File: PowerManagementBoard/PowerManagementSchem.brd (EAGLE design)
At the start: 160 x 100 mm, 100 parts, among them J1 D15S24A4GV00LF, J2 455-1750-1-ND, U1 VX7805-500, U2 PYB20-Q24-S5, U3 PYB30-Q48-S5, U4 PYB30-Q48-S12, U5 3V3REG, U6 INA4180-SPLIT, U7 INA4180-SPLIT, U8 TEENSY-4.0SILK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

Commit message: Initial board layout
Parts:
- moved U$20 793.9 mm to (161.3, 81.3), turned to 180 degrees
- moved R22 785.4 mm to (157.5, 78.7)
- moved J7 775.0 mm to (160.0, 30.5), turned to 90 degrees
- moved J6 733.6 mm to (120.7, 12.7), turned to 180 degrees
- moved J5 718.0 mm to (96.5, 12.7), turned to 180 degrees
- moved D12 712.9 mm to (128.3, 27.9), turned to 270 degrees
- moved U$23 704.2 mm to (134.6, 26.7)
- moved R21 703.1 mm to (128.3, 21.6), turned to 90 degrees
- moved D10 694.3 mm to (137.2, 41.9)
- moved J2 693.5 mm to (73.7, 12.7), turned to 180 degrees
- moved J4 692.9 mm to (53.3, 12.7), turned to 180 degrees
- moved D9 683.0 mm to (137.2, 34.3)
- moved J3 679.9 mm to (34.3, 12.7), turned to 180 degrees
- moved U9 669.6 mm to (138.4, 48.3)
- moved RN3 664.7 mm to (148.6, 27.9), turned to 180 degrees
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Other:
- board size 160 x 100 mm -> 165.1 x 106.3 mm

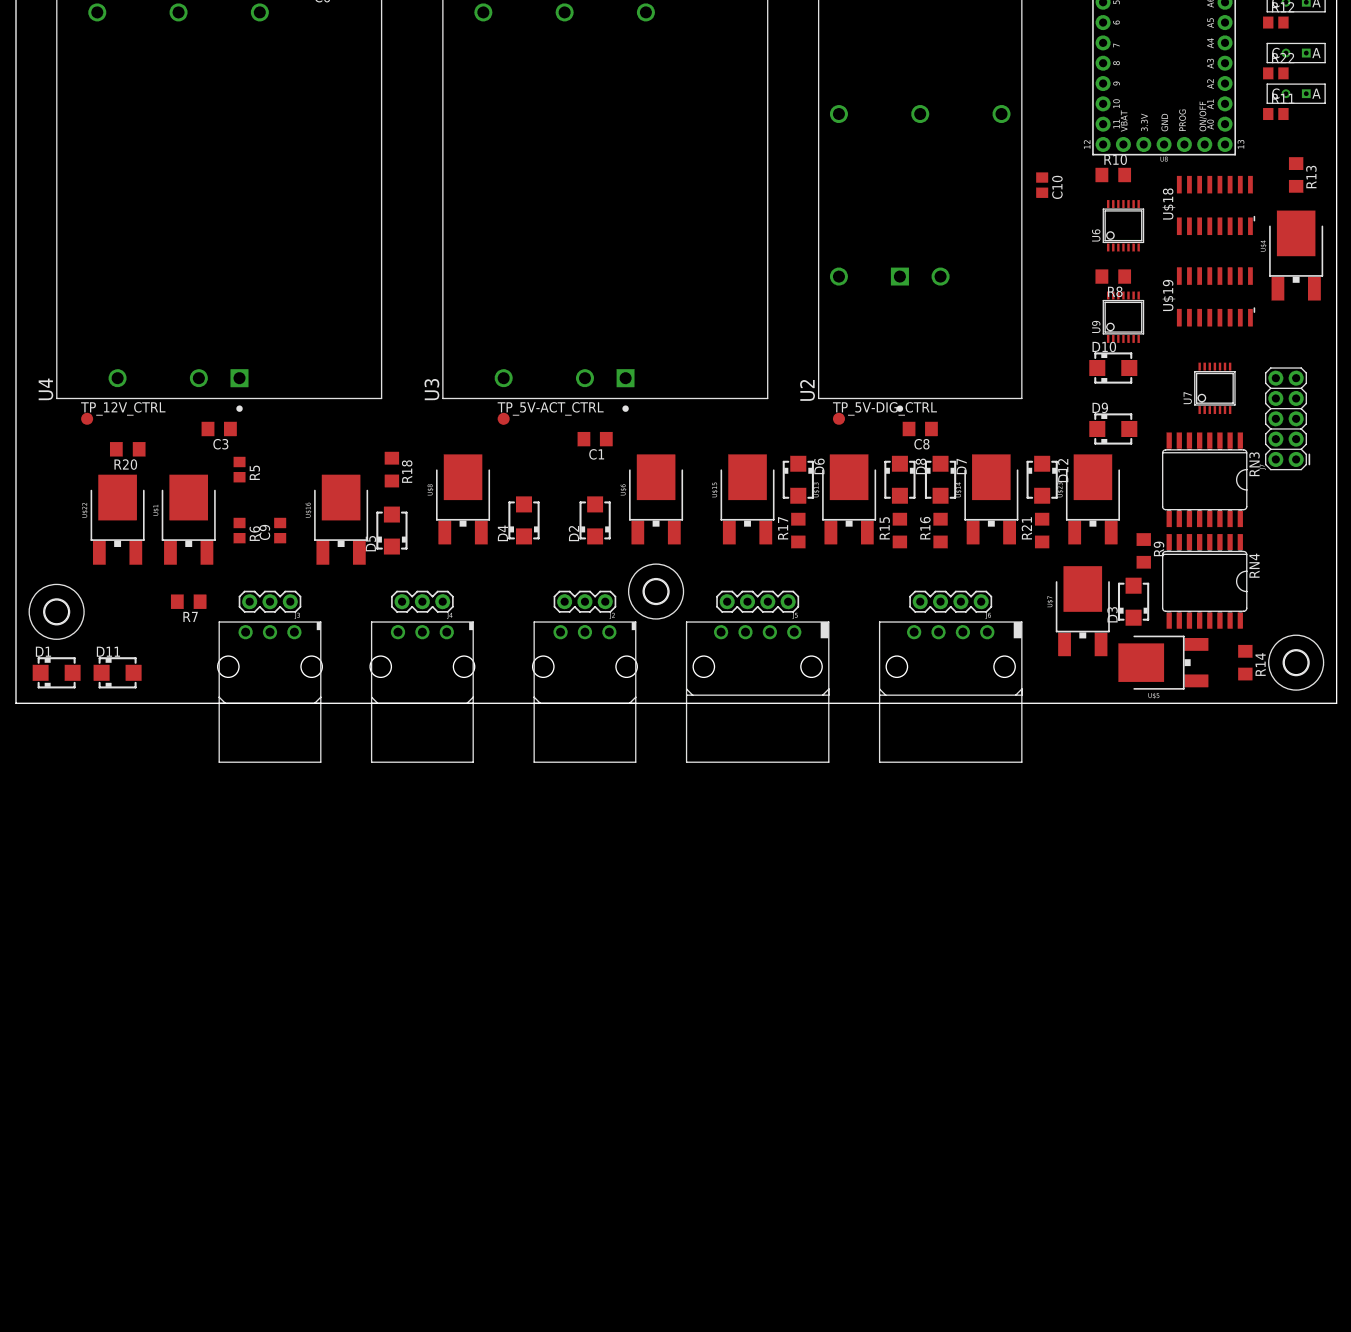
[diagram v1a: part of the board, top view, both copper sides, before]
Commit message: added db 37 and db25
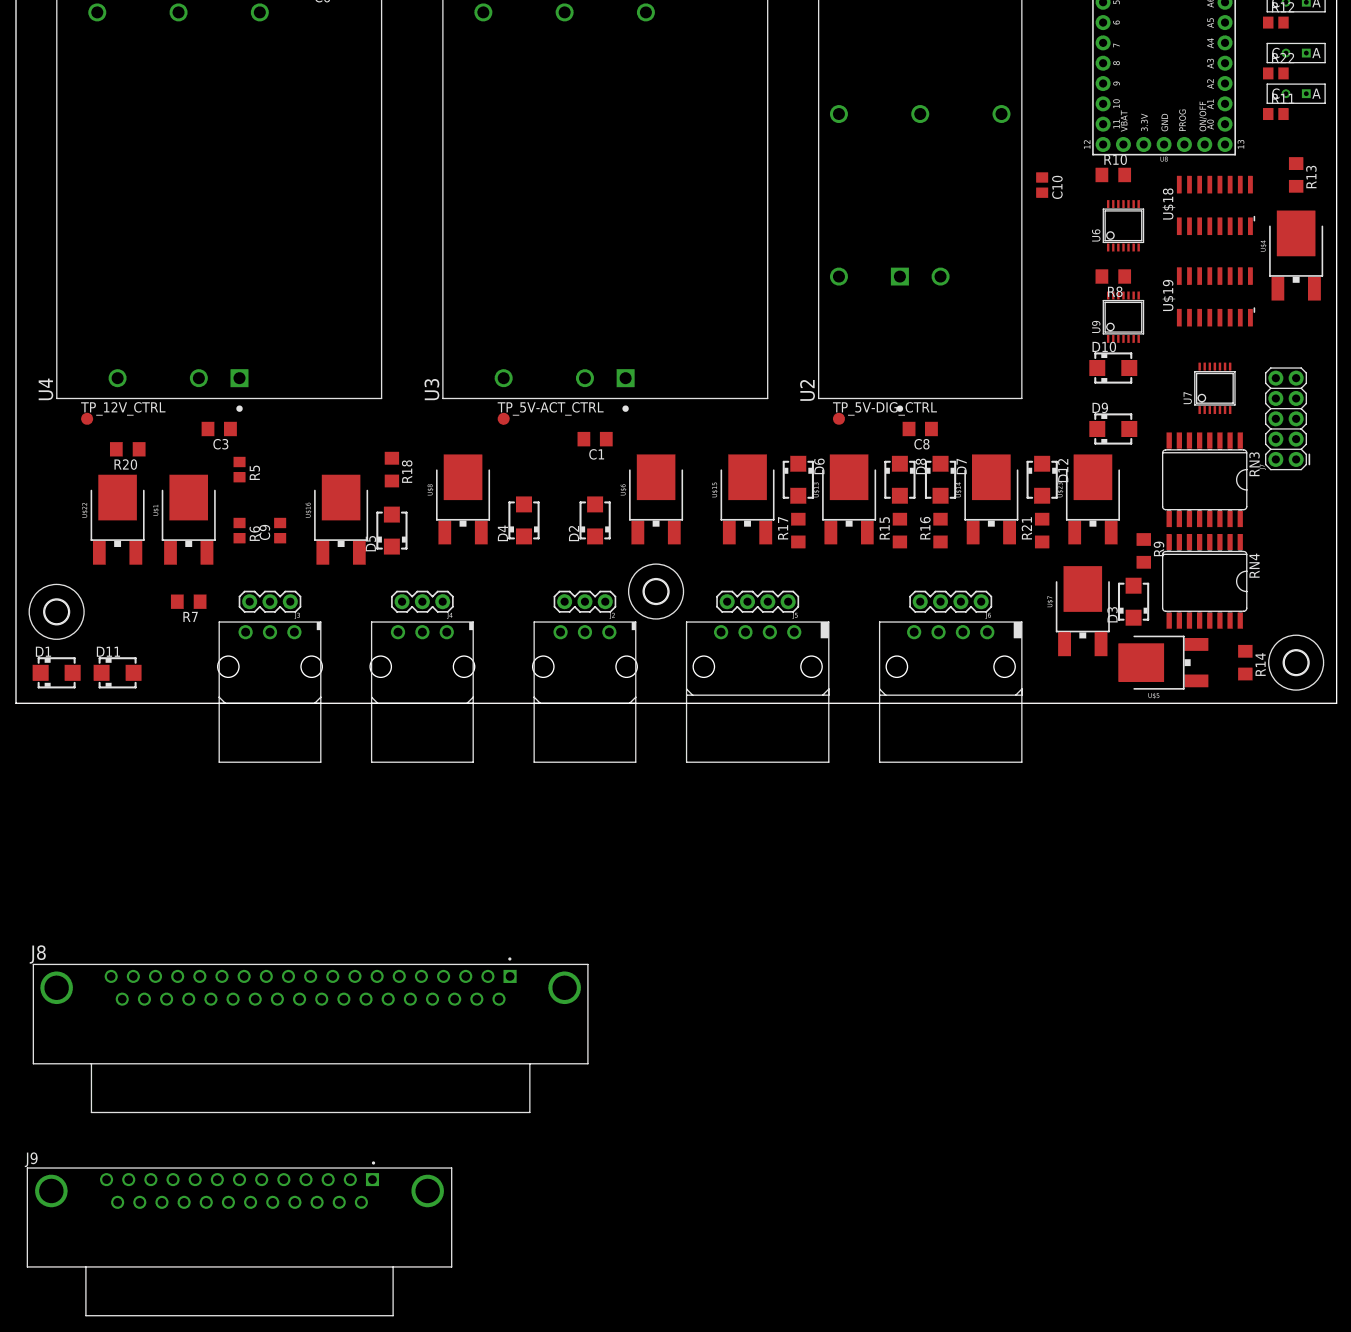
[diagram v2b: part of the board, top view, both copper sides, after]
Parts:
- added J8: 182-037-213R531, D-Sub Connectors:182-037-213R531
- added J9: 182-025-213R531, D-Sub Connectors:182-025-213R531
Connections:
- new net ANT-MISO: J8.30, J9.15
- new net ANT-MOSI: J8.29, J9.14
- new net ANT-SCK: J8.31, J9.16
- new net ANT-SS: J8.32, J9.17
- new net BOOM-I2C-SCL: J8.34, J9.13
- new net BOOM-I2C-SDA: J8.33, J9.12
- new net LASER-I2C-SCL: J8.10, J9.7
- new net LASER-I2C-SDA: J8.9, J9.6
- new net LASER-UART-1: J8.4, J9.1
- new net LASER-UART-2: J8.5, J9.2
- new net LASER-UART-3: J8.6, J9.3
- new net LASER-UART-4: J8.7, J9.4
- new net LASER-UART-5: J8.8, J9.5
- new net MAGNET-I2C-SCL: J8.21, J9.11
- new net MAGNET-I2C-SDA: J8.20, J9.10
- new net STATIC-I2C-SCL: J8.16, J9.9
- new net STATIC-I2C-SDA: J8.15, J9.8
- net 12V-CAM: now also J8.25
- net 12V-STA: now also J8.14
- net 5V-ACT-CAM: now also J8.24
- net 5V-ACT-LASER: now also J8.3
- net 5V-ACT-MAG: now also J8.19
- net 5V-ACT-STA: now also J8.13
- net 5V-ACT-TX: now also J8.28
- net 5V-DIG-CAM: now also J8.23, J9.24
- net 5V-DIG-LASER: now also J8.2, J9.21
- net 5V-DIG-MAG: now also J8.18, J9.23
- net 5V-DIG-STA: now also J8.12, J9.22
- net 5V-DIG-TX: now also J8.27, J9.25
- net GND: now also J8.1, J8.11, J8.17, J8.22, J8.26, J8.MH1, J8.MH2, J9.20

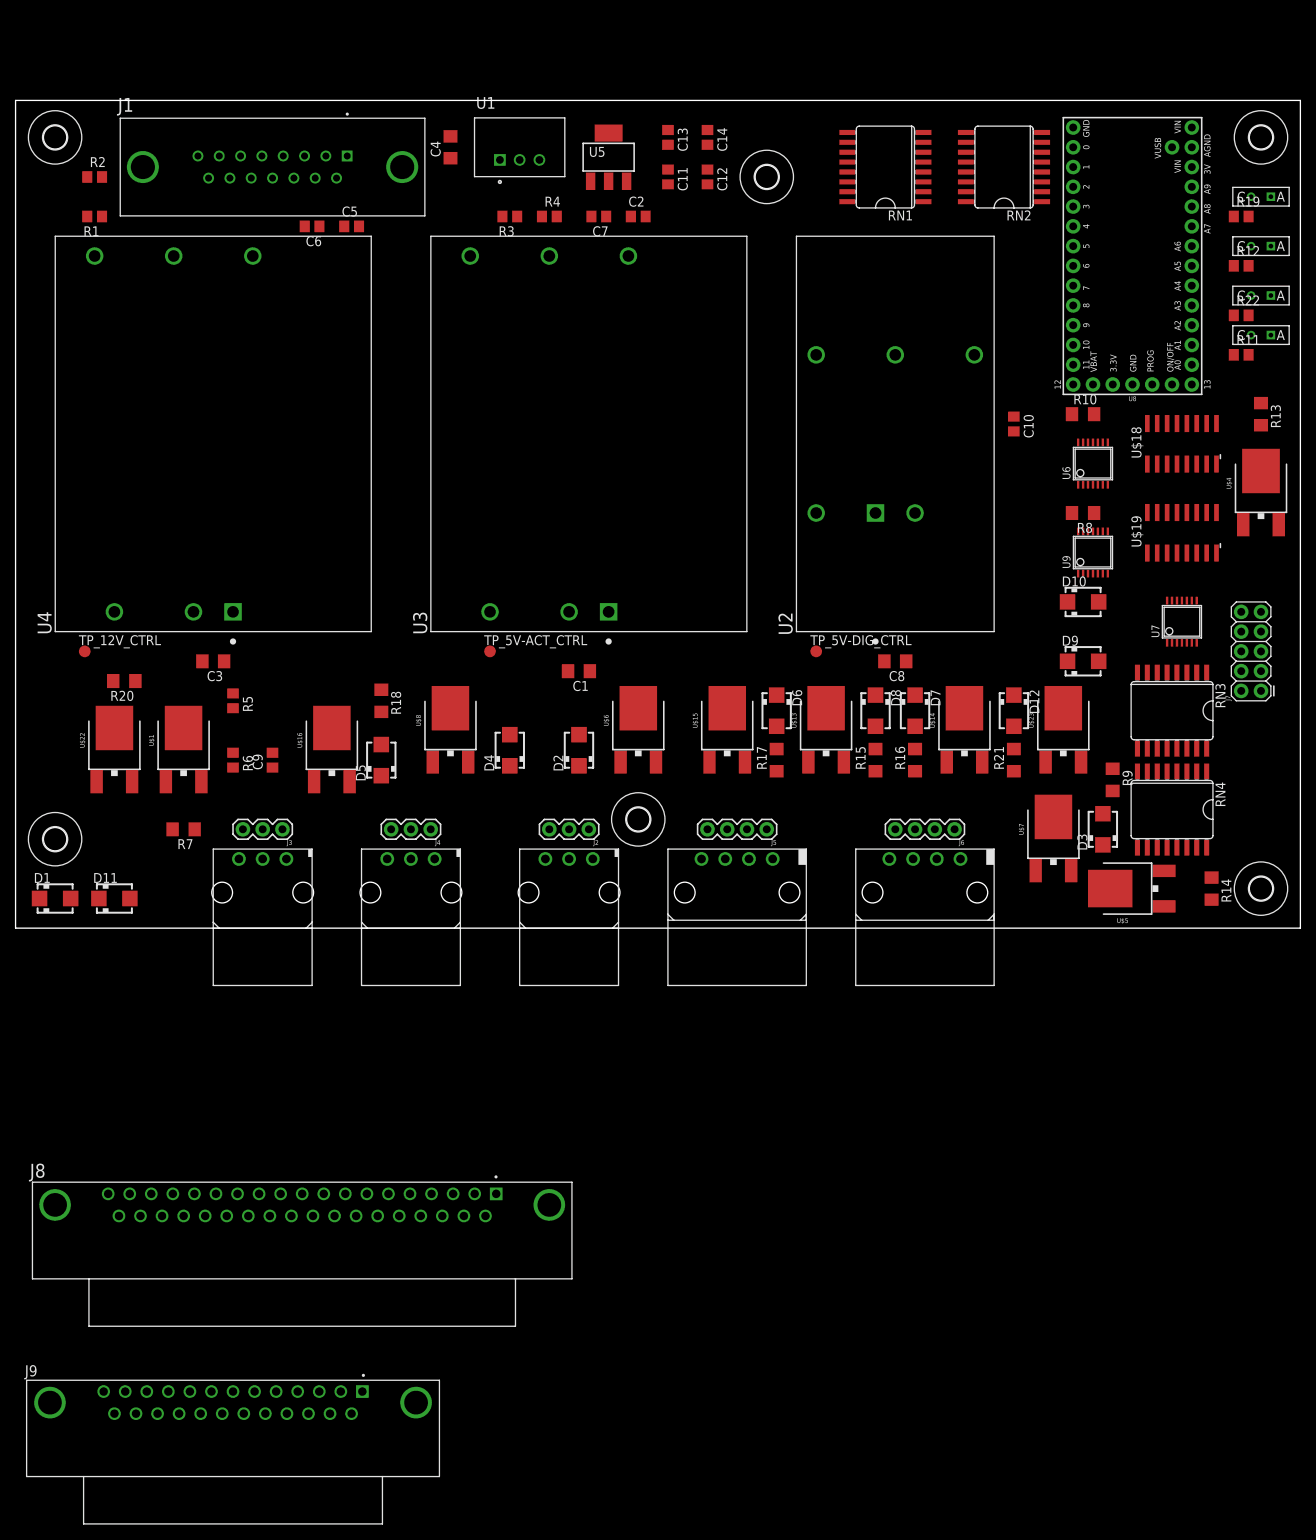
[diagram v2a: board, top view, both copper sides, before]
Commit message: Power Board: Removed molex connectors, started routing signals
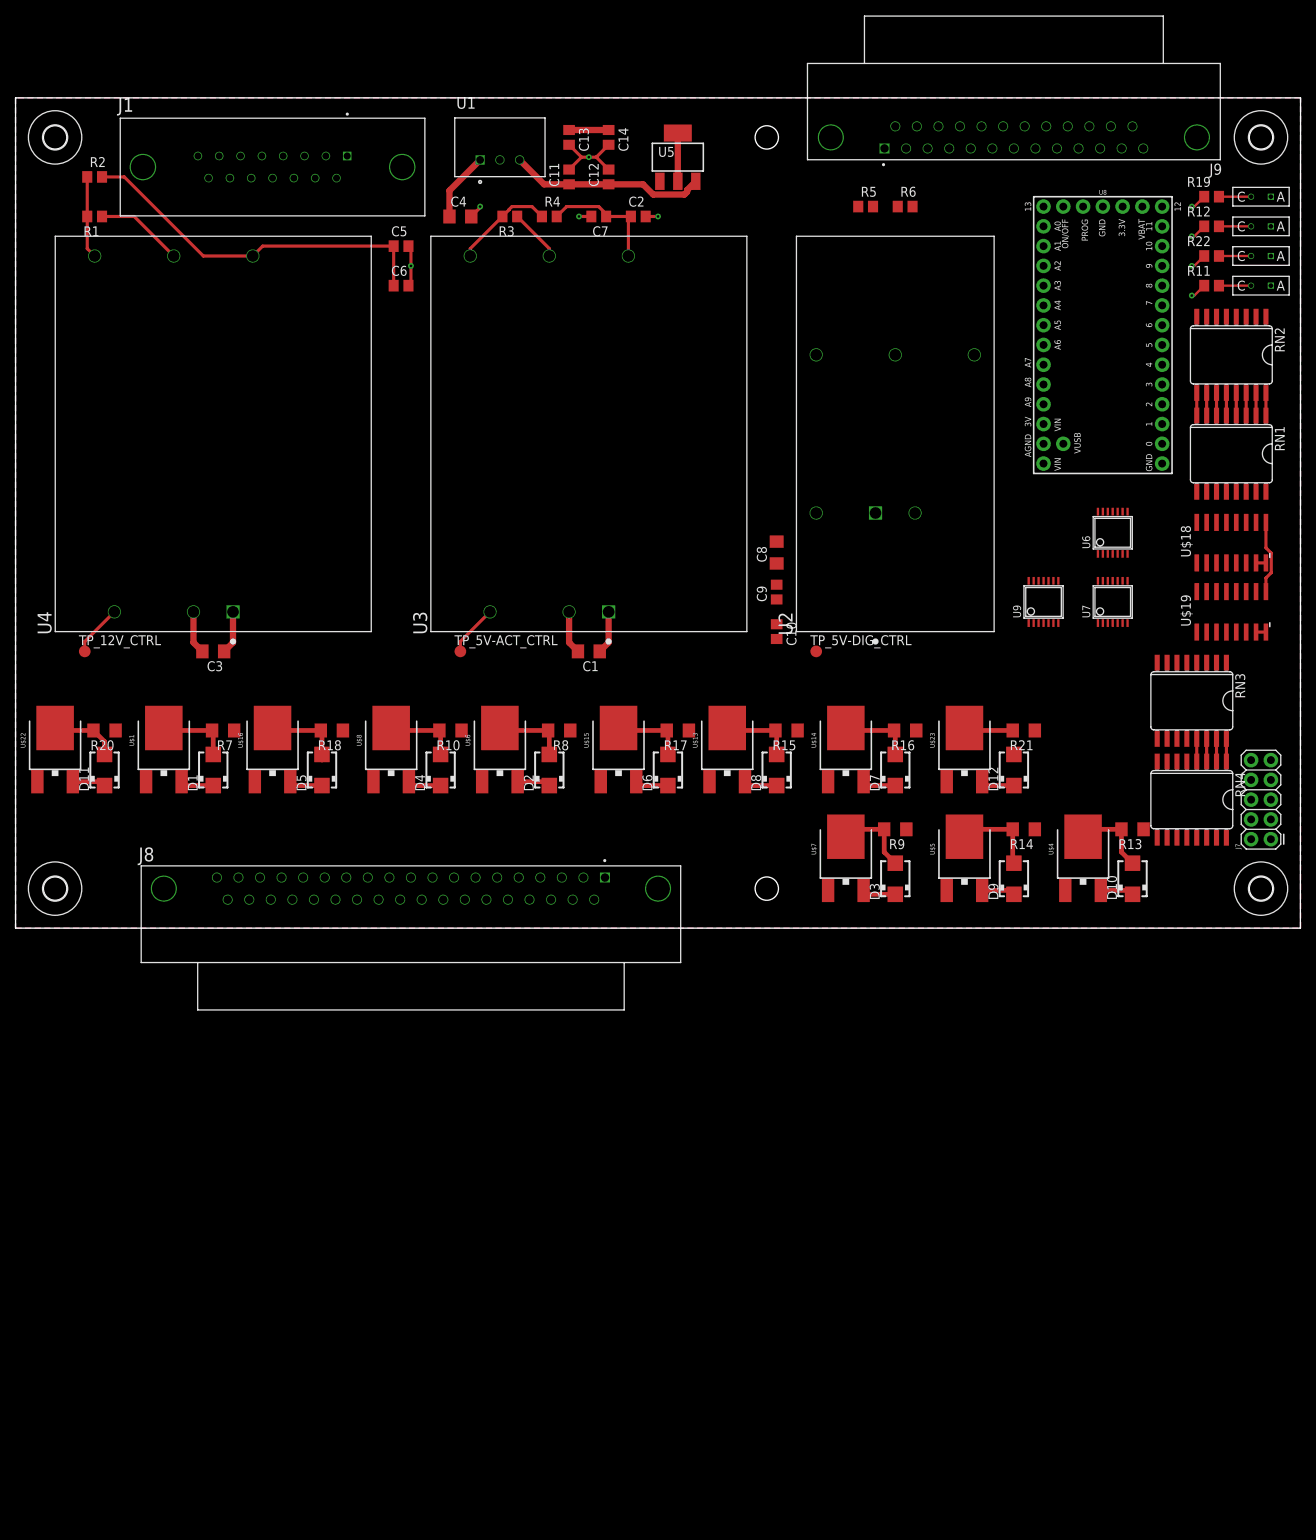
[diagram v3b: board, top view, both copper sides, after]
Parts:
- removed J2: 455-1750-1-ND, SparkFun-Connectors:1X03
- removed J3, J4: (no value), SparkFun-Connectors:1X03
- removed J5, J6: (no value), SparkFun-Connectors:1X04
- removed U$11, U$12: MOLEX_4PIN, PowerManagementParts:MOLEX_4PIN
- removed U$2, U$24, U$3: MOLEX_3PIN, PowerManagementParts:MOLEX_3PIN
- moved J9 191.0 mm to (128.3, 101.6), turned to 180 degrees
- moved R6 111.9 mm to (114.3, 92.7), turned to 0 degrees
- moved R5 103.1 mm to (109.2, 92.7), turned to 0 degrees
- moved R10 90.9 mm to (55.9, 25.4), turned to 180 degrees
- moved R8 72.9 mm to (69.8, 25.4)
- moved C9 68.3 mm to (97.8, 43.2)
- moved RN1 57.7 mm to (156.2, 61.0), turned to 180 degrees
- moved R13 55.8 mm to (143.5, 12.7), turned to 180 degrees
- moved U$4 52.3 mm to (137.2, 10.2)
- moved J8 43.0 mm to (50.8, 5.08)
- moved C10 40.5 mm to (97.8, 38.1)
- moved RN2 37.9 mm to (156.2, 73.7), turned to 180 degrees
- moved D10 36.1 mm to (143.5, 6.35), turned to 90 degrees
- moved D9 29.3 mm to (128.3, 6.35), turned to 90 degrees
- moved R9 28.7 mm to (113.0, 12.7), turned to 180 degrees
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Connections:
- net 12V: now also D11.C, D12.C
- net 12V-CAM: no longer J5.1, U$11.PIN1
- net 12V-STA: no longer J6.1, U$12.PIN1
- net 5V-ACT-CAM: no longer J5.3, U$11.PIN3
- net 5V-ACT-LASER: no longer J4.2, U$3.PIN2
- net 5V-ACT-MAG: no longer J2.2, U$24.PIN2
- net 5V-ACT-STA: no longer J6.3, U$12.PIN3
- net 5V-ACT-TX: no longer J3.2, U$2.PIN2
- net 5V-DIG: now also D1.C
- net 5V-DIG-CAM: no longer J5.4, U$11.PIN4
- net 5V-DIG-LASER: no longer J4.3, U$3.PIN3
- net 5V-DIG-MAG: no longer J2.3, U$24.PIN3
- net 5V-DIG-STA: no longer J6.4, U$12.PIN4
- net 5V-DIG-TX: no longer J3.3, U$2.PIN3
- net GND: no longer J2.1, J3.1, J4.1, J5.2, J6.2, U$11.PIN2, U$12.PIN2, U$2.PIN1, U$24.PIN1, U$3.PIN1
- net N$11: now also D1.A
- net N$34: now also D11.A
- net N$36: now also D12.A
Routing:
- net 12V: track 0.00 -> 55.8 mm
- net GND: track 0.00 -> 54.6 mm, vias 0 -> 9
- net 5V-ACT: track 0.00 -> 37.4 mm
- net MNGR-5V: track 0.00 -> 25.3 mm
- net 5V-DIG: track 0.00 -> 21.4 mm
- net N$4: track 0.00 -> 12.9 mm
- net MNGR-3.3V: track 0.00 -> 11.3 mm
- net N$3: track 0.00 -> 10.6 mm
- net N$32: track 0.00 -> 10.1 mm
- net N$22: track 0.00 -> 9.87 mm
- net N$16: track 0.00 -> 9.47 mm
- net N$11: track 0.00 -> 9.47 mm
- net N$28: track 0.00 -> 9.47 mm
- net MUX-SEL-C: track 0.00 -> 9.45 mm
- net N$24: track 0.00 -> 9.34 mm
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- added copper zone on layer 16, net GND
- added copper zone on layer 1, net MNGR-3.3V
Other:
- board size 165.1 x 106.3 mm -> 165.1 x 106.7 mm

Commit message: Added USB lines for the camera
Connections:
- new net CAM-USB-D+: J8.35, J9.18
- new net CAM-USB-D-: J8.36, J9.19
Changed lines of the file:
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@@
 <?xml version="1.0" encoding="utf-8"?>
 <!DOCTYPE eagle SYSTEM "eagle.dtd">
-<eagle version="9.5.2">
+<eagle version="9.4.2">
 <drawing>
 <settings>
@@
 <wire x1="60.495" y1="3.66" x2="121.345" y2="103.02" width="0" layer="19" extent="1-1"/>
 </signal>
+<signal name="CAM-USB-D+">
+<contactref element="J9" pad="18"/>
+<contactref element="J8" pad="35"/>
+<wire x1="68.805" y1="3.66" x2="124.115" y2="103.02" width="0" layer="19" extent="1-1"/>
+</signal>
+<signal name="CAM-USB-D-">
+<contactref element="J8" pad="36"/>
+<contactref element="J9" pad="19"/>
+<wire x1="71.575" y1="3.66" x2="126.885" y2="103.02" width="0" layer="19" extent="1-1"/>
+</signal>
 </signals>

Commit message: Reorganized MOSFETs
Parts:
- moved U$1 159.1 mm to (72.4, -125.7)
- moved D1 159.1 mm to (78.7, -129.5)
- moved R7 159.1 mm to (80.0, -124.5)
- moved R8 154.8 mm to (50.8, -128.3)
- moved D2 154.8 mm to (49.5, -133.3)
- moved U$6 154.8 mm to (43.2, -129.5)
- moved D12 133.9 mm to (19.1, -57.1)
- moved R21 133.9 mm to (20.3, -52.1)
- moved U$23 133.9 mm to (12.7, -53.3)
- moved D5 130.5 mm to (78.7, -104.1)
- moved R18 130.5 mm to (80.0, -99.1)
- moved U$16 130.5 mm to (72.4, -100.3)
- moved R17 126.1 mm to (48.3, -95.2)
- moved U$15 126.1 mm to (40.6, -96.5)
- moved D6 126.1 mm to (47.0, -100.3)
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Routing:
- net GND: track 54.6 -> 58.6 mm, vias 9 -> 10
- net N$3: track 10.6 -> 8.01 mm
- net 12V: track 55.8 -> 57.6 mm
- net MNGR-5V: track 25.3 -> 26.0 mm
- net N$34: track 8.60 -> 8.07 mm
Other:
- outline, holes or cut-outs redrawn
- board text added: "12V"
- board text added: "5V-ACT"
- board text added: "5V-DIG"
- board text added: "Ant"
- board text added: "Boom"
- board text added: "Laser"
- board text added: "MAG"
- board text added: "Routing Plan: -Start by arranging MOSFETS in the best possible configuration. Spending time here will save time later -Place other components (like resistor arrays and op amps). Don't worry about small vregs yet -Route big power traces, route traces that go near mosfets -Now, place minor components like small vregs in the free space"
- board text added: "Static"
